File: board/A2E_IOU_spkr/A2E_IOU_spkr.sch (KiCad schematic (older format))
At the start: 3 parts, among them J1 IOU_Socket, J2 PCB_Socket, U1 GAL16V8

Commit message: Base pcb for GAL
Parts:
- added C1: 100nF, Capacitor_THT:C_Disc_D4.3mm_W1.9mm_P5.00mm, symbol Device:C_Small
- added J3: Test, Connector_PinHeader_2.54mm:PinHeader_1x02_P2.54mm_Vertical, symbol Connector_Generic:Conn_01x02
- J1, J2: footprint (none) -> Package_DIP:DIP-40_W15.24mm
- U1: footprint (none) -> Package_DIP:DIP-20_W7.62mm
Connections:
- net GND: now also U1.10 (GND), U1.11 (I10/~OE~), U1.7 (I7), U1.8 (I8), U1.9 (I9), C1.2, J3.2 (Pin_2)
- net ORA4: now also U1.6 (I6)
- net ORA5: now also U1.5 (I5)
- net ORA6: now also U1.4 (I4)
- net ORA7: now also U1.3 (I3)
- net PHI0: now also U1.1 (I1/CLK)
- net SPKR: no longer J2.8 (Pin_8)
- net VCC: now also U1.20 (VCC), C1.1
- net ~C0XX: now also U1.2 (I2)
- net N_SPKR: now reaches U1.19 (IO1)
- net N_SPKR: now also J2.8 (Pin_8), J3.1 (Pin_1)
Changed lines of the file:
@@
 F 0 "J1" H 2750 3267 50  0000 C CNN
 F 1 "IOU_Socket" H 2750 3176 50  0000 C CNN
-F 2 "" H 2700 2150 50  0001 C CNN
+F 2 "Package_DIP:DIP-40_W15.24mm" H 2700 2150 50  0001 C CNN
 F 3 "~" H 2700 2150 50  0001 C CNN
 	1    2700 2150
@@
 F 0 "J2" H 4700 3267 50  0000 C CNN
 F 1 "PCB_Socket" H 4700 3176 50  0000 C CNN
-F 2 "" H 4650 2150 50  0001 C CNN
+F 2 "Package_DIP:DIP-40_W15.24mm" H 4650 2150 50  0001 C CNN
 F 3 "~" H 4650 2150 50  0001 C CNN
 	1    4650 2150
@@
 F 0 "U1" H 6950 2800 50  0000 C CNN
 F 1 "GAL16V8" H 7450 2800 50  0000 C CNN
-F 2 "" H 7200 2150 50  0001 C CNN
+F 2 "Package_DIP:DIP-20_W7.62mm" H 7200 2150 50  0001 C CNN
 F 3 "" H 7200 2150 50  0001 C CNN
 	1    7200 2150
@@
 A6
 Text Label 4100 1950 0    50   ~ 0
-SPKR
+N_SPKR
 Text Label 4100 1850 0    50   ~ 0
 CASS0
@@
 Text Label 2150 3150 0    50   ~ 0
 ORA3
+Wire Wire Line
+	7700 1650 8150 1650
+Text Label 8150 1650 2    50   ~ 0
+N_SPKR
+$Comp
+L power:GND #PWR?
+U 1 1 5F8CB968
+P 7200 2950
+F 0 "#PWR?" H 7200 2700 50  0001 C CNN
+F 1 "GND" H 7205 2777 50  0000 C CNN
+F 2 "" H 7200 2950 50  0001 C CNN
+F 3 "" H 7200 2950 50  0001 C CNN
+	1    7200 2950
+	1    0    0    -1
+$EndComp
+Wire Wire Line
+	7200 2850 7200 2900
+$Comp
+L power:VCC #PWR?
+U 1 1 5F8CFE6B
+P 7200 1350
+F 0 "#PWR?" H 7200 1200 50  0001 C CNN
+F 1 "VCC" H 7215 1523 50  0000 C CNN
+F 2 "" H 7200 1350 50  0001 C CNN
+F 3 "" H 7200 1350 50  0001 C CNN
+	1    7200 1350
+	1    0    0    -1
+$EndComp
+Wire Wire Line
+	7200 1350 7200 1450
+Wire Wire Line
+	6700 1650 6150 1650
+Wire Wire Line
+	6700 1750 6150 1750
+Wire Wire Line
+	6700 1850 6150 1850
+Wire Wire Line
+	6700 1950 6150 1950
+Wire Wire Line
+	6700 2050 6150 2050
+Wire Wire Line
+	6700 2150 6150 2150
+Text Label 6150 1650 0    50   ~ 0
+PHI0
+Text Label 6150 1750 0    50   ~ 0
+~C0XX
+Text Label 6150 1850 0    50   ~ 0
+ORA7
+Text Label 6150 1950 0    50   ~ 0
+ORA6
+Text Label 6150 2050 0    50   ~ 0
+ORA5
+Text Label 6150 2150 0    50   ~ 0
+ORA4
+Wire Wire Line
+	6700 2250 6550 2250
+Wire Wire Line
+	6550 2250 6550 2350
+Wire Wire Line
+	6550 2900 7200 2900
+Connection ~ 7200 2900
+Wire Wire Line
+	7200 2900 7200 2950
+Wire Wire Line
+	6700 2350 6550 2350
+Connection ~ 6550 2350
+Wire Wire Line
+	6550 2350 6550 2450
+Wire Wire Line
+	6700 2450 6550 2450
+Connection ~ 6550 2450
+Wire Wire Line
+	6550 2450 6550 2550
+Wire Wire Line
+	6700 2550 6550 2550
+Connection ~ 6550 2550
+Wire Wire Line
+	6550 2550 6550 2900
+$Comp
+L Device:C_Small C1
+U 1 1 5F900106
+P 8650 1800
+F 0 "C1" H 8742 1846 50  0000 L CNN
+F 1 "100nF" H 8742 1755 50  0000 L CNN
+F 2 "Capacitor_THT:C_Disc_D4.3mm_W1.9mm_P5.00mm" H 8650 1800 50  0001 C CNN
+F 3 "~" H 8650 1800 50  0001 C CNN
+	1    8650 1800
+	1    0    0    -1
+$EndComp
+$Comp
+L power:VCC #PWR?
+U 1 1 5F900898
+P 8650 1600
+F 0 "#PWR?" H 8650 1450 50  0001 C CNN
+F 1 "VCC" H 8665 1773 50  0000 C CNN
+F 2 "" H 8650 1600 50  0001 C CNN
+F 3 "" H 8650 1600 50  0001 C CNN
+	1    8650 1600
+	1    0    0    -1
+$EndComp
+$Comp
+L power:GND #PWR?
+U 1 1 5F900F58
+P 8650 2000
+F 0 "#PWR?" H 8650 1750 50  0001 C CNN
+F 1 "GND" H 8655 1827 50  0000 C CNN
+F 2 "" H 8650 2000 50  0001 C CNN
+F 3 "" H 8650 2000 50  0001 C CNN
+	1    8650 2000
+	1    0    0    -1
+$EndComp
+Wire Wire Line
+	8650 1600 8650 1700
+Wire Wire Line
+	8650 1900 8650 2000
+$Comp
+L Connector_Generic:Conn_01x02 J3
+U 1 1 5F90AF40
+P 9600 1650
+F 0 "J3" H 9680 1642 50  0000 L CNN
+F 1 "Test" H 9680 1551 50  0000 L CNN
+F 2 "Connector_PinHeader_2.54mm:PinHeader_1x02_P2.54mm_Vertical" H 9600 1650 50  0001 C CNN
+F 3 "~" H 9600 1650 50  0001 C CNN
+	1    9600 1650
+	1    0    0    -1
+$EndComp
+$Comp
+L power:GND #PWR?
+U 1 1 5F90B4F6
+P 9250 1800
+F 0 "#PWR?" H 9250 1550 50  0001 C CNN
+F 1 "GND" H 9255 1627 50  0000 C CNN
+F 2 "" H 9250 1800 50  0001 C CNN
+F 3 "" H 9250 1800 50  0001 C CNN
+	1    9250 1800
+	1    0    0    -1
+$EndComp
+Wire Wire Line
+	9400 1750 9250 1750
+Wire Wire Line
+	9250 1750 9250 1800
+Wire Wire Line
+	9400 1650 9050 1650
+Text Label 9050 1650 0    50   ~ 0
+N_SPKR
 $EndSCHEMATC

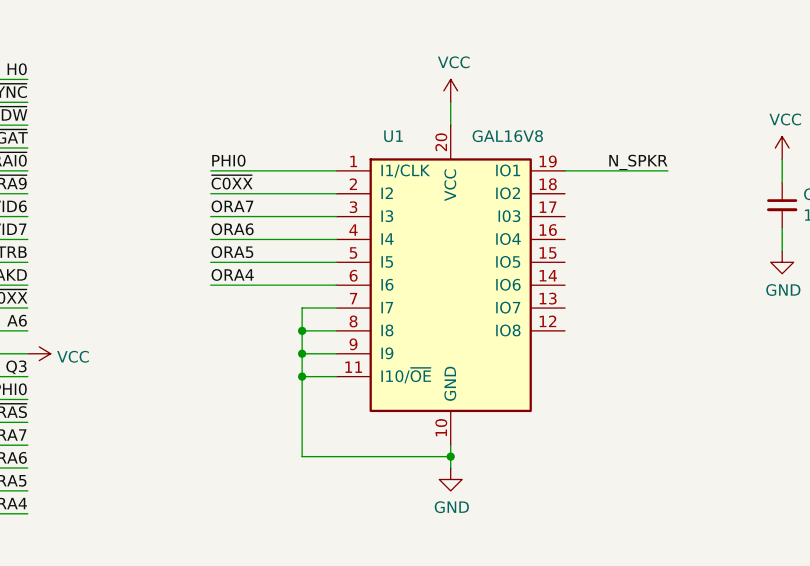
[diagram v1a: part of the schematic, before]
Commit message: Update eqn and schematics
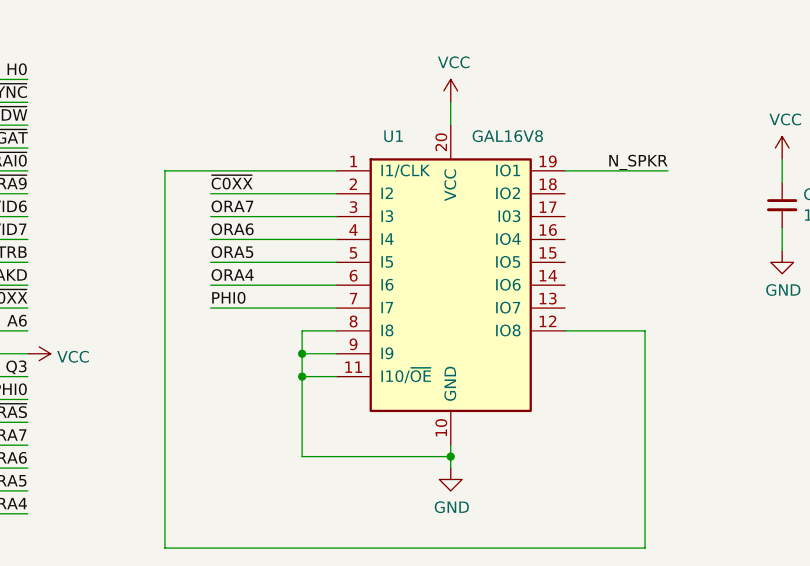
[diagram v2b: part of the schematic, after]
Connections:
- net GND: no longer U1.7 (I7)
- net PHI0: now also U1.7 (I7); no longer U1.1 (I1/CLK)
- net at U1.12 (IO8): now also U1.1 (I1/CLK)
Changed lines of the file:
@@
 	5350 3150 4950 3150
-$Comp
-L Logic_Programmable:GAL16V8 U1
-U 1 1 5F92C8C7
-P 7200 2150
-F 0 "U1" H 6950 2800 50  0000 C CNN
-F 1 "GAL16V8" H 7450 2800 50  0000 C CNN
-F 2 "Package_DIP:DIP-20_W7.62mm" H 7200 2150 50  0001 C CNN
-F 3 "" H 7200 2150 50  0001 C CNN
-	1    7200 2150
-	1    0    0    -1
-$EndComp
 $Comp
 L power:GND #PWR?
@@
 Wire Wire Line
 	7200 1350 7200 1450
-Wire Wire Line
-	6700 1650 6150 1650
-Wire Wire Line
-	6700 1750 6150 1750
-Wire Wire Line
-	6700 1850 6150 1850
-Wire Wire Line
-	6700 1950 6150 1950
-Wire Wire Line
-	6700 2050 6150 2050
-Wire Wire Line
-	6700 2150 6150 2150
-Text Label 6150 1650 0    50   ~ 0
+Text Label 6150 2250 0    50   ~ 0
 PHI0
 Text Label 6150 1750 0    50   ~ 0
@@
 ORA4
 Wire Wire Line
-	6700 2250 6550 2250
-Wire Wire Line
-	6550 2250 6550 2350
-Wire Wire Line
 	6550 2900 7200 2900
 Connection ~ 7200 2900
@@
 	7200 2900 7200 2950
 Wire Wire Line
-	6700 2350 6550 2350
-Connection ~ 6550 2350
-Wire Wire Line
-	6550 2350 6550 2450
-Wire Wire Line
-	6700 2450 6550 2450
-Connection ~ 6550 2450
-Wire Wire Line
 	6550 2450 6550 2550
-Wire Wire Line
-	6700 2550 6550 2550
 Connection ~ 6550 2550
 Wire Wire Line
@@
 Text Label 9050 1650 0    50   ~ 0
 N_SPKR
+Connection ~ 6550 2450
+Wire Wire Line
+	6700 2550 6550 2550
+Wire Wire Line
+	6700 2450 6550 2450
+Wire Wire Line
+	6700 2150 6150 2150
+Wire Wire Line
+	6700 2050 6150 2050
+Wire Wire Line
+	6700 1950 6150 1950
+Wire Wire Line
+	6700 1850 6150 1850
+Wire Wire Line
+	6700 1750 6150 1750
+Wire Wire Line
+	6700 2250 6150 2250
+Wire Wire Line
+	6550 2350 6550 2450
+Wire Wire Line
+	6700 2350 6550 2350
+$Comp
+L Logic_Programmable:GAL16V8 U1
+U 1 1 5F92C8C7
+P 7200 2150
+F 0 "U1" H 6950 2800 50  0000 C CNN
+F 1 "GAL16V8" H 7450 2800 50  0000 C CNN
+F 2 "Package_DIP:DIP-20_W7.62mm" H 7200 2150 50  0001 C CNN
+F 3 "" H 7200 2150 50  0001 C CNN
+	1    7200 2150
+	1    0    0    -1
+$EndComp
+Wire Wire Line
+	7700 2350 8050 2350
+Wire Wire Line
+	8050 2350 8050 3300
+Wire Wire Line
+	8050 3300 5950 3300
+Wire Wire Line
+	5950 3300 5950 1650
+Wire Wire Line
+	5950 1650 6700 1650
 $EndSCHEMATC

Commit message: Update schematics
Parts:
- removed J3: Test, Connector_PinHeader_2.54mm:PinHeader_1x02_P2.54mm_Vertical, symbol Connector_Generic:Conn_01x02
- added C2: 100nF, Capacitor_THT:C_Disc_D4.3mm_W1.9mm_P5.00mm, symbol Device:C_Small
- added U2: 74LS373, symbol 74xx:74LS373
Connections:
- net A6: now also U1.4 (I4)
- net GND: now also C2.2, U2.1 (OE), U2.10 (GND); no longer U1.11 (I10/~OE~), U1.8 (I8), U1.9 (I9)
- net N_SPKR: now also U1.17 (I03); no longer U1.19 (IO1)
- net ORA0: now also U2.3 (D0)
- net ORA1: now also U2.4 (D1)
- net ORA2: now also U2.7 (D2)
- net ORA3: now also U2.8 (D3)
- net ORA4: now also U2.13 (D4); no longer U1.6 (I6)
- net ORA5: now also U2.14 (D5); no longer U1.5 (I5)
- net ORA6: now also U2.17 (D6); no longer U1.4 (I4)
- net ORA7: no longer U1.3 (I3)
- net PHI0: now also U1.2 (I2); no longer U1.7 (I7)
- net Q3: now also U1.5 (I5)
- net VCC: now also C2.1, U2.20 (VCC)
- net ~C0XX: now also U1.9 (I9); no longer U1.2 (I2)
- net ~PRAS: now also U1.3 (I3)
- net SPKR_TTL: now reaches U1.18 (IO2)
- new net ADDR_LATCH: U1.19 (IO1), U2.11 (LE)
- new net LA0: U2.2 (O0)
- new net LA1: U2.5 (O1)
- new net LA2: U2.6 (O2)
- new net LA3: U2.9 (O3)
- new net LA4: U1.7 (I7), U2.12 (O4)
- new net LA5: U1.8 (I8), U2.15 (O5)
- new net LA7: U1.6 (I6), U2.16 (O6)
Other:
- moved on the sheet: U1

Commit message: Updated PCB
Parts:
- U2: footprint (none) -> Package_DIP:DIP-20_W7.62mm
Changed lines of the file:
@@
 	5350 3150 4950 3150
 $Comp
-L power:GND #PWR?
+L power:GND #PWR0101
 U 1 1 5F92D5F3
 P 4100 1250
-F 0 "#PWR?" H 4100 1000 50  0001 C CNN
+F 0 "#PWR0101" H 4100 1000 50  0001 C CNN
 F 1 "GND" V 4105 1122 50  0000 R CNN
 F 2 "" H 4100 1250 50  0001 C CNN
@@
 $EndComp
 $Comp
-L power:VCC #PWR?
+L power:VCC #PWR0102
 U 1 1 5F93E7EC
 P 5350 2450
-F 0 "#PWR?" H 5350 2300 50  0001 C CNN
+F 0 "#PWR0102" H 5350 2300 50  0001 C CNN
 F 1 "VCC" V 5365 2578 50  0000 L CNN
 F 2 "" H 5350 2450 50  0001 C CNN
@@
 	3400 3150 3000 3150
 $Comp
-L power:VCC #PWR?
+L power:VCC #PWR0103
 U 1 1 5F94903A
 P 3400 2450
-F 0 "#PWR?" H 3400 2300 50  0001 C CNN
+F 0 "#PWR0103" H 3400 2300 50  0001 C CNN
 F 1 "VCC" V 3415 2578 50  0000 L CNN
 F 2 "" H 3400 2450 50  0001 C CNN
@@
 	2500 3150 2150 3150
 $Comp
-L power:GND #PWR?
+L power:GND #PWR0104
 U 1 1 5F94CEE7
 P 2150 1250
-F 0 "#PWR?" H 2150 1000 50  0001 C CNN
+F 0 "#PWR0104" H 2150 1000 50  0001 C CNN
 F 1 "GND" V 2155 1122 50  0000 R CNN
 F 2 "" H 2150 1250 50  0001 C CNN
@@
 ORA3
 $Comp
-L power:GND #PWR?
+L power:GND #PWR0105
 U 1 1 5F8CB968
 P 4800 5550
-F 0 "#PWR?" H 4800 5300 50  0001 C CNN
+F 0 "#PWR0105" H 4800 5300 50  0001 C CNN
 F 1 "GND" H 4805 5377 50  0000 C CNN
 F 2 "" H 4800 5550 50  0001 C CNN
@@
 $EndComp
 $Comp
-L power:VCC #PWR?
+L power:VCC #PWR0106
 U 1 1 5F8CFE6B
 P 4800 3950
-F 0 "#PWR?" H 4800 3800 50  0001 C CNN
+F 0 "#PWR0106" H 4800 3800 50  0001 C CNN
 F 1 "VCC" H 4815 4123 50  0000 C CNN
 F 2 "" H 4800 3950 50  0001 C CNN
@@
 $EndComp
 $Comp
-L power:VCC #PWR?
+L power:VCC #PWR0107
 U 1 1 5F900898
 P 8650 1600
-F 0 "#PWR?" H 8650 1450 50  0001 C CNN
+F 0 "#PWR0107" H 8650 1450 50  0001 C CNN
 F 1 "VCC" H 8665 1773 50  0000 C CNN
 F 2 "" H 8650 1600 50  0001 C CNN
@@
 $EndComp
 $Comp
-L power:GND #PWR?
+L power:GND #PWR0108
 U 1 1 5F900F58
 P 8650 2000
-F 0 "#PWR?" H 8650 1750 50  0001 C CNN
+F 0 "#PWR0108" H 8650 1750 50  0001 C CNN
 F 1 "GND" H 8655 1827 50  0000 C CNN
 F 2 "" H 8650 2000 50  0001 C CNN
@@
 F 0 "U2" H 8400 5400 50  0000 C CNN
 F 1 "74LS373" H 8900 5400 50  0000 C CNN
-F 2 "" H 8650 4700 50  0001 C CNN
+F 2 "Package_DIP:DIP-20_W7.62mm" H 8650 4700 50  0001 C CNN
 F 3 "http://www.ti.com/lit/gpn/sn74LS373" H 8650 4700 50  0001 C CNN
 	1    8650 4700
@@
 $EndComp
 $Comp
-L power:GND #PWR?
+L power:GND #PWR0109
 U 1 1 5F95611C
 P 8650 5600
-F 0 "#PWR?" H 8650 5350 50  0001 C CNN
+F 0 "#PWR0109" H 8650 5350 50  0001 C CNN
 F 1 "GND" H 8655 5427 50  0000 C CNN
 F 2 "" H 8650 5600 50  0001 C CNN
@@
 $EndComp
 $Comp
-L power:VCC #PWR?
+L power:VCC #PWR0110
 U 1 1 5F9663C8
 P 9150 1600
-F 0 "#PWR?" H 9150 1450 50  0001 C CNN
+F 0 "#PWR0110" H 9150 1450 50  0001 C CNN
 F 1 "VCC" H 9165 1773 50  0000 C CNN
 F 2 "" H 9150 1600 50  0001 C CNN
@@
 $EndComp
 $Comp
-L power:GND #PWR?
+L power:GND #PWR0111
 U 1 1 5F9663D2
 P 9150 2000
-F 0 "#PWR?" H 9150 1750 50  0001 C CNN
+F 0 "#PWR0111" H 9150 1750 50  0001 C CNN
 F 1 "GND" H 9155 1827 50  0000 C CNN
 F 2 "" H 9150 2000 50  0001 C CNN
@@
 ~PRAS
 $Comp
-L power:VCC #PWR?
+L power:VCC #PWR0112
 U 1 1 5F9941BE
 P 8650 3800
-F 0 "#PWR?" H 8650 3650 50  0001 C CNN
+F 0 "#PWR0112" H 8650 3650 50  0001 C CNN
 F 1 "VCC" H 8665 3973 50  0000 C CNN
 F 2 "" H 8650 3800 50  0001 C CNN
